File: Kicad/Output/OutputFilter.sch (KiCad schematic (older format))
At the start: 6 parts

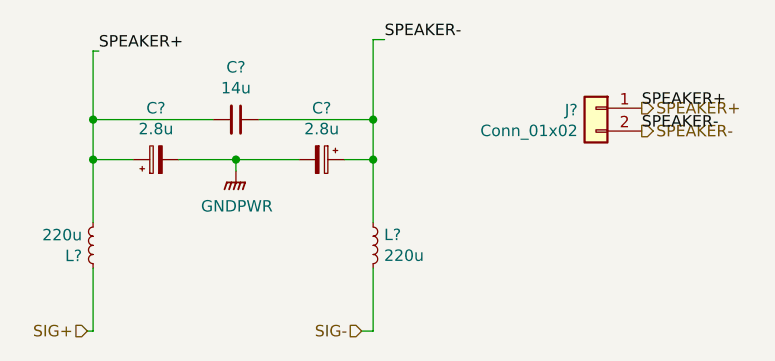
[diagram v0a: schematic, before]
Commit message: Prepared O/P Filter PCB for track layout
Laid out components for Output Filter PCB compactly ready for tracks to be drawn. Have drawn out precise margin lines too.
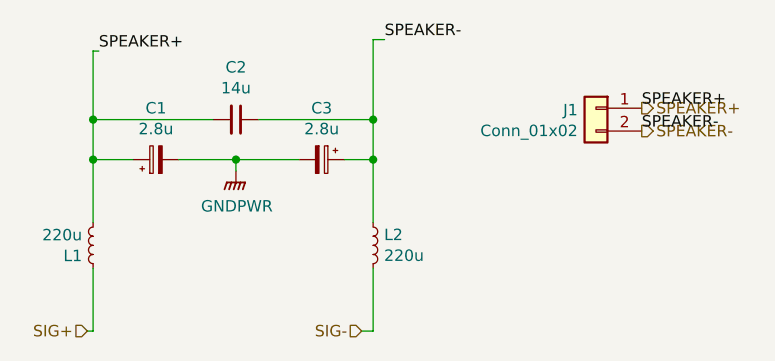
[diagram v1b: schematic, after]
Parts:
- gave numbers to parts that had none: 6
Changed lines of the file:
@@
 $Descr A4 11693 8268
 encoding utf-8
-Sheet 2 6
+Sheet 2 2
 Title ""
 Date ""
@@
 $EndDescr
 $Comp
-L Device:L_Small L?
+L Device:L_Small L2
 U 1 1 61155806
 P 5975 3225
-F 0 "L?" H 6023 3271 50  0000 L CNN
+F 0 "L2" H 6023 3271 50  0000 L CNN
 F 1 "220u" H 6023 3180 50  0000 L CNN
 F 2 "1422455C:1422455C" H 5975 3225 50  0001 C CNN
@@
 $EndComp
 $Comp
-L Device:C_Small C?
+L Device:C_Small C2
 U 1 1 61156022
 P 5375 2675
-F 0 "C?" V 5146 2675 50  0000 C CNN
+F 0 "C2" V 5146 2675 50  0000 C CNN
 F 1 "14u" V 5237 2675 50  0000 C CNN
 F 2 "OutputFilmCapacitor:C4AQQBW5140A3JJ" H 5375 2675 50  0001 C CNN
@@
 $EndComp
 $Comp
-L Device:CP_Small C?
+L Device:CP_Small C3
 U 1 1 61156A03
 P 5750 2850
-F 0 "C?" V 5525 2850 50  0000 C CNN
+F 0 "C3" V 5525 2850 50  0000 C CNN
 F 1 "2.8u" V 5616 2850 50  0000 C CNN
 F 2 "Capacitor_THT:CP_Radial_D8.0mm_P3.50mm" H 5750 2850 50  0001 C CNN
@@
 	5975 3600 5925 3600
 $Comp
-L power:GNDPWR #PWR?
+L power:GNDPWR #PWR0101
 U 1 1 6115D61E
 P 5375 2900
-F 0 "#PWR?" H 5375 2700 50  0001 C CNN
+F 0 "#PWR0101" H 5375 2700 50  0001 C CNN
 F 1 "GNDPWR" H 5379 2746 50  0000 C CNN
 F 2 "" H 5375 2850 50  0001 C CNN
@@
 	5375 2850 5650 2850
 $Comp
-L Device:L_Small L?
+L Device:L_Small L1
 U 1 1 61202529
 P 4750 3225
-F 0 "L?" H 4798 3271 50  0000 L CNN
+F 0 "L1" H 4798 3271 50  0000 L CNN
 F 1 "220u" H 4798 3180 50  0000 L CNN
 F 2 "1422455C:1422455C" H 4750 3225 50  0001 C CNN
@@
 $EndComp
 $Comp
-L Device:CP_Small C?
+L Device:CP_Small C1
 U 1 1 61203FC8
 P 5025 2850
-F 0 "C?" V 5250 2850 50  0000 C CNN
+F 0 "C1" V 5250 2850 50  0000 C CNN
 F 1 "2.8u" V 5159 2850 50  0000 C CNN
 F 2 "Capacitor_THT:CP_Radial_D8.0mm_P3.50mm" H 5025 2850 50  0001 C CNN
@@
 $EndComp
 $Comp
-L Connector_Generic:Conn_01x02 J?
+L Connector_Generic:Conn_01x02 J1
 U 1 1 610FED81
 P 6950 2625
-F 0 "J?" H 7030 2617 50  0000 L CNN
+F 0 "J1" H 7030 2617 50  0000 L CNN
 F 1 "Conn_01x02" H 7030 2526 50  0000 L CNN
 F 2 "TerminalBlock:TerminalBlock_bornier-2_P5.08mm" H 6950 2625 50  0001 C CNN

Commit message: OP Filter PCB Done
OP Filter PCB finished
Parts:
- L1, L2: footprint 1422455C:1422455C -> OutputInductor:IND_HCTI-220-5.8
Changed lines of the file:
@@
 F 0 "L2" H 6023 3271 50  0000 L CNN
 F 1 "220u" H 6023 3180 50  0000 L CNN
-F 2 "1422455C:1422455C" H 5975 3225 50  0001 C CNN
+F 2 "OutputInductor:IND_HCTI-220-5.8" H 5975 3225 50  0001 C CNN
 F 3 "~" H 5975 3225 50  0001 C CNN
 	1    5975 3225
@@
 F 0 "L1" H 4798 3271 50  0000 L CNN
 F 1 "220u" H 4798 3180 50  0000 L CNN
-F 2 "1422455C:1422455C" H 4750 3225 50  0001 C CNN
+F 2 "OutputInductor:IND_HCTI-220-5.8" H 4750 3225 50  0001 C CNN
 F 3 "~" H 4750 3225 50  0001 C CNN
 	1    4750 3225

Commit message: Make Output Filter Board Smaller
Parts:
- C2: footprint OutputFilmCapacitor:C4AQQBW5140A3JJ -> OutputFilmCapacitor:C4AQLBU5140M18K
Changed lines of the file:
@@
 F 0 "C2" V 5146 2675 50  0000 C CNN
 F 1 "14u" V 5237 2675 50  0000 C CNN
-F 2 "OutputFilmCapacitor:C4AQQBW5140A3JJ" H 5375 2675 50  0001 C CNN
+F 2 "OutputFilmCapacitor:C4AQLBU5140M18K" H 5375 2675 50  0001 C CNN
 F 3 "~" H 5375 2675 50  0001 C CNN
 	1    5375 2675
